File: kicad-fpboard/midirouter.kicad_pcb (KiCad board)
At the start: 2 copper layers, 42.5 x 90 mm, 45 parts, among them J1 MIDI_IN_1, J10 Conn_01x08, J2 MIDI_IN_2, J3 MIDI_IN_3, J4 MIDI_IN_4, J5 Conn_01x08, J6 MIDI_OUT_1, J7 MIDI_OUT_2, J8 MIDI_OUT_3, J9 MIDI_OUT_4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

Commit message: Work on schematics and pcbs.
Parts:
- removed the REF** at (95.0, 132.0)
- added L1: 1k@100mhz, Inductor_SMD:L_0603_1608Metric_Pad1.05x0.95mm_HandSolder, B.Cu at (86.5, 75.2)
- added L10: 1k@100mhz, Inductor_SMD:L_0603_1608Metric_Pad1.05x0.95mm_HandSolder, B.Cu at (108.0, 142.0)
- added L11: 1k@100mhz, Inductor_SMD:L_0603_1608Metric_Pad1.05x0.95mm_HandSolder, B.Cu at (104.0, 119.8)
- added L12: 1k@100mhz, Inductor_SMD:L_0603_1608Metric_Pad1.05x0.95mm_HandSolder, B.Cu at (108.0, 119.8)
- added L13: 1k@100mhz, Inductor_SMD:L_0603_1608Metric_Pad1.05x0.95mm_HandSolder, B.Cu at (104.0, 98.0)
- added L14: 1k@100mhz, Inductor_SMD:L_0603_1608Metric_Pad1.05x0.95mm_HandSolder, B.Cu at (108.0, 98.0)
- added L15: 1k@100mhz, Inductor_SMD:L_0603_1608Metric_Pad1.05x0.95mm_HandSolder, B.Cu at (104.0, 76.0)
- added L16: 1k@100mhz, Inductor_SMD:L_0603_1608Metric_Pad1.05x0.95mm_HandSolder, B.Cu at (108.0, 76.0)
- added L2: 1k@100mhz, Inductor_SMD:L_0603_1608Metric_Pad1.05x0.95mm_HandSolder, B.Cu at (80.8, 143.2)
- added L3: 1k@100mhz, Inductor_SMD:L_0603_1608Metric_Pad1.05x0.95mm_HandSolder, B.Cu at (86.8, 141.5)
- added L4: 1k@100mhz, Inductor_SMD:L_0603_1608Metric_Pad1.05x0.95mm_HandSolder, B.Cu at (80.8, 121.2)
- added L5: 1k@100mhz, Inductor_SMD:L_0603_1608Metric_Pad1.05x0.95mm_HandSolder, B.Cu at (86.8, 119.5)
- added L6: 1k@100mhz, Inductor_SMD:L_0603_1608Metric_Pad1.05x0.95mm_HandSolder, B.Cu at (80.8, 99.2)
- added L7: 1k@100mhz, Inductor_SMD:L_0603_1608Metric_Pad1.05x0.95mm_HandSolder, B.Cu at (86.5, 97.5)
- added L8: 1k@100mhz, Inductor_SMD:L_0603_1608Metric_Pad1.05x0.95mm_HandSolder, B.Cu at (80.5, 77.0)
- added L9: 1k@100mhz, Inductor_SMD:L_0603_1608Metric_Pad1.05x0.95mm_HandSolder, B.Cu at (104.0, 142.0)
- added REF**: MountingHole_3.2mm_M3, MountingHole:MountingHole_3.2mm_M3, F.Cu at (106.0, 88.0)
- added REF**: MountingHole_3.2mm_M3, MountingHole:MountingHole_3.2mm_M3, F.Cu at (84.0, 132.0)
- added REF**: MountingHole_3.2mm_M3, MountingHole:MountingHole_3.2mm_M3, F.Cu at (106.0, 132.0)
- C1, C2, C3, C4: footprint Capacitor_SMD:C_1206_3216Metric_Pad1.42x1.75mm_HandSolder -> Capacitor_SMD:C_0805_2012Metric
- D1, D2, D3, D4: footprint Diode_SMD:D_1206_3216Metric_Pad1.42x1.75mm_HandSolder -> Diode_SMD:D_0805_2012Metric
- R1, R10, R11, R12, R13, R14, R15, R16, R2, R3, R4, R5, R6, R7, R8, R9: footprint Resistor_SMD:R_1206_3216Metric_Pad1.42x1.75mm_HandSolder -> Resistor_SMD:R_0805_2012Metric
- U1: footprint Package_SO:SOP-16_7.5x10.4mm_P1.27mm -> Package_SO:SOP-16_4.4x10.4mm_P1.27mm
- moved REF** 11.0 mm to (84.0, 88.0)
- moved C3 5.00 mm to (83.2, 95.8)
- moved C2 4.92 mm to (83.2, 117.8)
- moved C4 4.88 mm to (83.2, 73.8)
- moved C1 4.85 mm to (83.2, 139.8)
- moved R4 3.75 mm to (83.5, 101.2)
- moved R3 3.66 mm to (83.5, 123.2)
- moved R2 3.57 mm to (83.5, 145.2)
- moved R5 3.35 mm to (83.5, 79.0)
- moved R6 2.47 mm to (101.2, 109.0)
- moved R1 2.40 mm to (101.2, 111.5)
- moved D4 1.92 mm to (85.2, 77.0), turned to 0 degrees
- moved D1 1.74 mm to (85.2, 143.2), turned to 0 degrees
- moved D2 1.72 mm to (85.2, 121.2), turned to 0 degrees
- moved D3 1.65 mm to (85.2, 99.2), turned to 0 degrees
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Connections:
- J1 pad 5: Net-(D1-Pad2) -> Net-(J1-Pad5)
- J2 pad 5: Net-(D2-Pad2) -> Net-(J2-Pad5)
- J3 pad 5: Net-(D3-Pad2) -> Net-(J3-Pad5)
- J4 pad 5: Net-(D4-Pad2) -> Net-(J4-Pad5)
- R10 pad 1: Net-(J7-Pad4) -> Net-(L11-Pad1)
- R11 pad 1: Net-(J8-Pad4) -> Net-(L13-Pad1)
- R12 pad 1: Net-(J9-Pad4) -> Net-(L15-Pad1)
- R13 pad 2: Net-(J6-Pad5) -> Net-(L10-Pad2)
- R14 pad 2: Net-(J7-Pad5) -> Net-(L12-Pad2)
- R15 pad 2: Net-(J8-Pad5) -> Net-(L14-Pad2)
- R16 pad 2: Net-(J9-Pad5) -> Net-(L16-Pad2)
- R2 pad 2: Net-(J1-Pad4) -> Net-(L2-Pad2)
- R3 pad 2: Net-(J2-Pad4) -> Net-(L4-Pad2)
- R4 pad 2: Net-(J3-Pad4) -> Net-(L6-Pad2)
- R5 pad 2: Net-(J4-Pad4) -> Net-(L8-Pad2)
- R9 pad 1: Net-(J6-Pad4) -> Net-(L9-Pad1)
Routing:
- net GND: track 40.1 -> 10.7 mm, vias 7 -> 8
- net LED1: track 89.0 -> 77.8 mm, vias 1 -> 3
- net MIDI_IN_2: track 31.3 -> 40.9 mm, vias 1 -> 0
- net Net-(D3-Pad2): track 19.6 -> 10.5 mm
- net LEDK2: track 109.6 -> 101.9 mm, vias 0 -> 1
- net Net-(D1-Pad1): track 41.3 -> 48.9 mm, vias 0 -> 2
- net MIDI_OUT_1: track 26.7 -> 19.1 mm, vias 2 -> 1
- net Net-(D1-Pad2): track 43.6 -> 36.6 mm
- net MIDI_OUT_3: track 45.3 -> 39.1 mm
- net Net-(D4-Pad2): track 36.9 -> 31.6 mm
- net MIDI_OUT_4: track 71.1 -> 66.0 mm
- net +3V3: track 119.6 -> 114.5 mm, vias 2 -> 0
- net Net-(D2-Pad2): track 20.7 -> 16.4 mm
- net LEDK1: track 73.3 -> 69.0 mm
- net MIDI_IN_3: track 45.2 -> 41.7 mm
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
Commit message: More work on pcbs and frontpanel.
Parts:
- moved D10 14.9 mm to (99.2, 91.0), turned to 180 degrees
- moved D12 14.9 mm to (99.2, 69.0), turned to 180 degrees
- moved D6 14.9 mm to (99.2, 135.0), turned to 180 degrees
- moved D8 14.9 mm to (99.2, 113.0), turned to 180 degrees
- moved R7 7.60 mm to (102.0, 106.0), turned to 0 degrees
- moved R8 7.20 mm to (102.0, 104.0), turned to 0 degrees
- moved D11 2.36 mm to (90.8, 69.0)
- moved D5 2.36 mm to (90.8, 135.0)
- moved D7 2.36 mm to (90.8, 113.0)
- moved D9 2.36 mm to (90.8, 91.0)
- moved U1 2.00 mm to (95.0, 105.0)
- moved R1 1.68 mm to (102.0, 110.0)
- moved R6 1.29 mm to (102.0, 108.0)
- moved R10 0.75 mm to (104.0, 122.2)
- moved R14 0.75 mm to (108.0, 122.2)
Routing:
- net LED2: track 57.6 -> 34.4 mm, vias 1 -> 0
- net LEDK2: track 101.9 -> 79.1 mm, vias 1 -> 2
- net LED3: track 33.9 -> 11.8 mm, vias 2 -> 0
- net LED1: track 77.8 -> 55.8 mm, vias 3 -> 2
- net +3V3: track 114.5 -> 94.3 mm
- net LED4: track 40.6 -> 21.8 mm
- net MIDI_IN_2: track 40.9 -> 28.2 mm
- net MIDI_IN_3: track 41.7 -> 31.5 mm
- net MIDI_IN_4: track 32.8 -> 24.4 mm
- net LEDK1: track 69.0 -> 77.3 mm, vias 0 -> 2
- net Net-(D1-Pad2): track 36.6 -> 40.6 mm
- net Net-(D1-Pad1): track 48.9 -> 45.4 mm, vias 2 -> 0
- net MIDI_OUT_3: track 39.1 -> 35.8 mm
- net Net-(D4-Pad2): track 31.6 -> 29.2 mm
- net Net-(D2-Pad2): track 16.4 -> 18.7 mm
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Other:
- board size 42.5 x 90 mm -> 39 x 85 mm

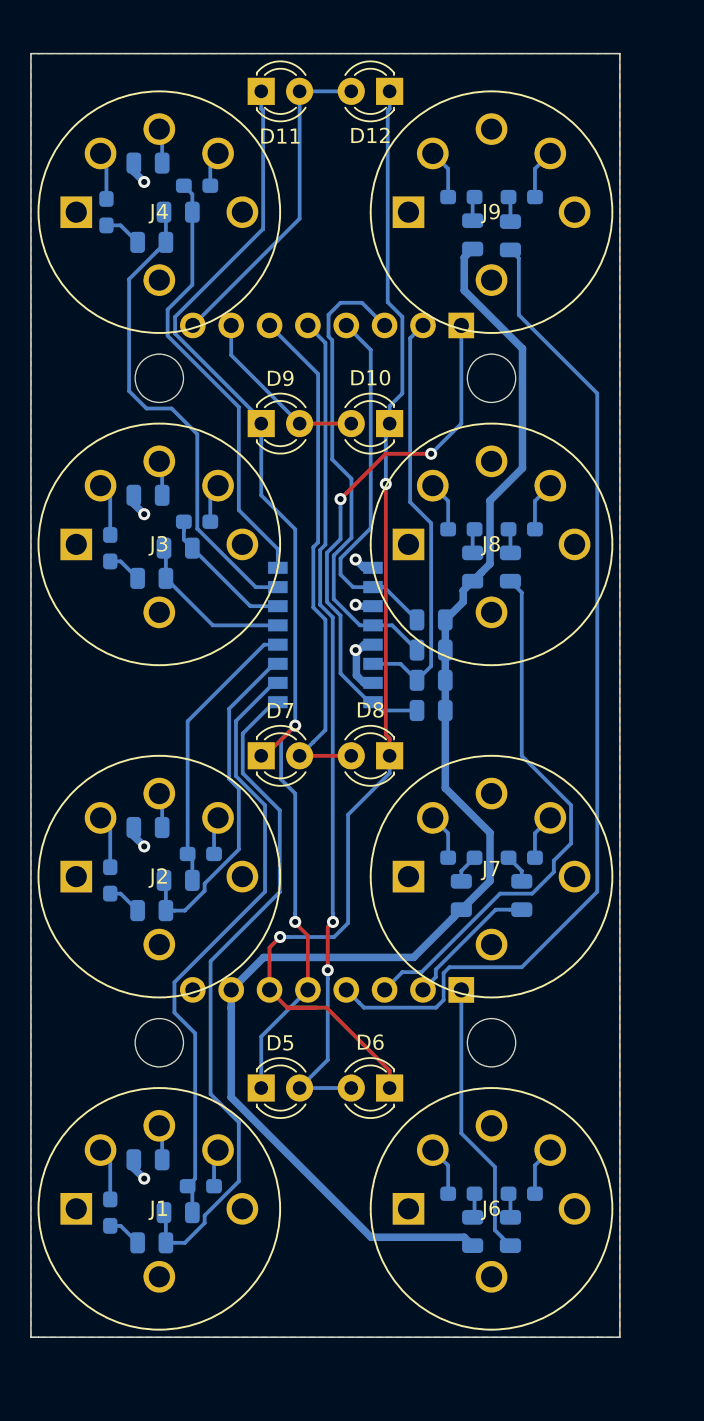
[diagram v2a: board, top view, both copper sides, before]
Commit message: Switch to TCMT4600 and increase size of ferrites.
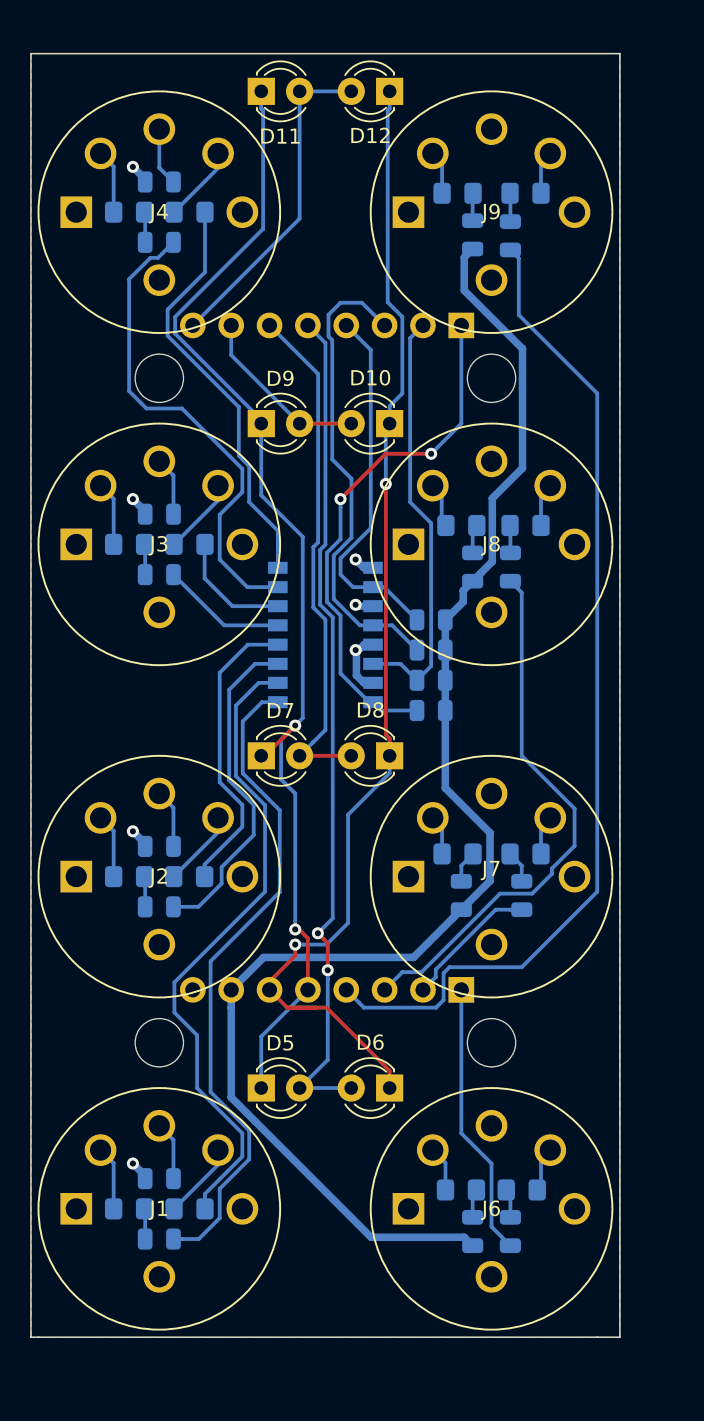
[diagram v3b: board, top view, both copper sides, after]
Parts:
- removed D1, D2, D3, D4: 1N4001, Diode_SMD:D_0805_2012Metric
- L1, L10, L11, L12, L13, L14, L15, L16, L2, L3, L4, L5, L6, L7, L8, L9: footprint Inductor_SMD:L_0603_1608Metric_Pad1.05x0.95mm_HandSolder -> Inductor_SMD:L_0805_2012Metric_Pad1.15x1.40mm_HandSolder
- U1: value PC847 -> TCMT4600
- moved L1 1.82 mm to (86.0, 77.0), turned to 0 degrees
- moved L5 1.69 mm to (86.0, 121.0), turned to 0 degrees
- moved L3 1.68 mm to (86.0, 143.0), turned to 0 degrees
- moved L7 1.58 mm to (86.0, 99.0), turned to 0 degrees
- moved L8 1.50 mm to (82.0, 77.0), turned to 0 degrees
- moved C1 1.46 mm to (84.0, 141.0)
- moved C2 1.46 mm to (84.0, 119.0)
- moved C3 1.46 mm to (84.0, 97.0)
- moved C4 1.46 mm to (84.0, 75.0)
- moved L2 1.27 mm to (82.0, 143.0), turned to 0 degrees
- moved L4 1.27 mm to (82.0, 121.0), turned to 0 degrees
- moved L6 1.27 mm to (82.0, 99.0), turned to 0 degrees
- moved R2 0.56 mm to (84.0, 145.0)
- moved R3 0.56 mm to (84.0, 123.0)
- moved R4 0.56 mm to (84.0, 101.0)
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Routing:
- net Net-(J4-Pad5): track 2.35 -> 5.83 mm
- net Net-(J3-Pad5): track 2.60 -> 5.83 mm
- net Net-(J2-Pad5): track 2.50 -> 5.48 mm
- net Net-(J1-Pad5): track 2.50 -> 5.47 mm
- net Net-(R4-Pad1): track 10.8 -> 8.30 mm
- net Net-(L3-Pad2): track 40.6 -> 42.9 mm
- net Net-(C4-Pad1): track 2.33 -> 4.15 mm
- net Net-(C3-Pad1): track 2.33 -> 4.15 mm
- net Net-(C2-Pad1): track 2.33 -> 4.15 mm
- net Net-(C1-Pad1): track 2.33 -> 4.15 mm
- net Net-(L1-Pad2): track 29.2 -> 27.6 mm
- net Net-(J3-Pad4): track 3.53 -> 5.15 mm
- net Net-(J2-Pad4): track 3.53 -> 5.15 mm
- net Net-(J4-Pad4): track 3.18 -> 4.80 mm
- net Net-(J1-Pad4): track 3.53 -> 5.15 mm
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
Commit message: Updates to frontpanels, schematics and pcbs.
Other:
- board text added: "."
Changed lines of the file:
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@@
   (general
     (thickness 1.6)
-    (drawings 13)
+    (drawings 14)
     (tracks 370)
     (zones 0)
@@
     )
   )
+  (gr_text . (at 93.25 108.75) (layer B.SilkS)
+    (effects (font (size 1.5 1.5) (thickness 0.3)) (justify mirror))
+  )
   (dimension 85 (width 0.3) (layer F.Fab)
